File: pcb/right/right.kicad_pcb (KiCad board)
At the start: 2 copper layers, 33 x 71.1 mm, 21 parts

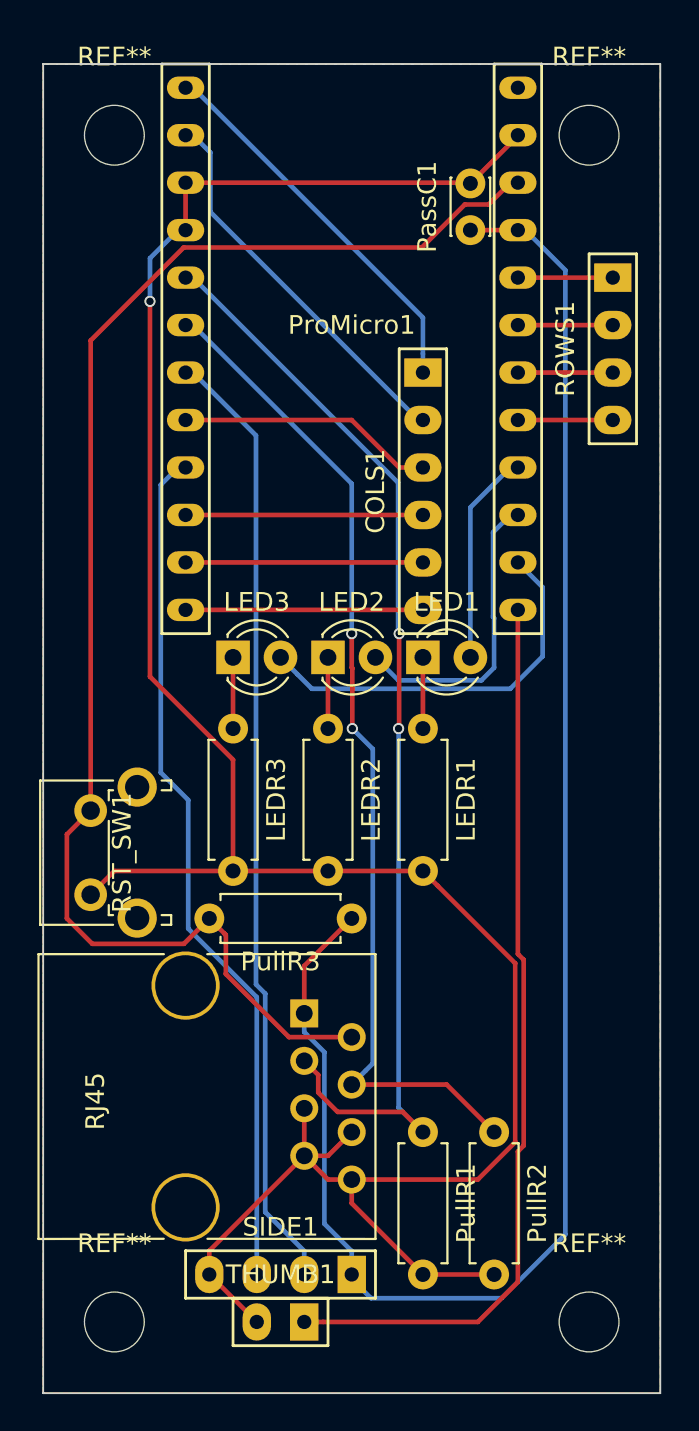
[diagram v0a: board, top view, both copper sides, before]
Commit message: fix pcb size
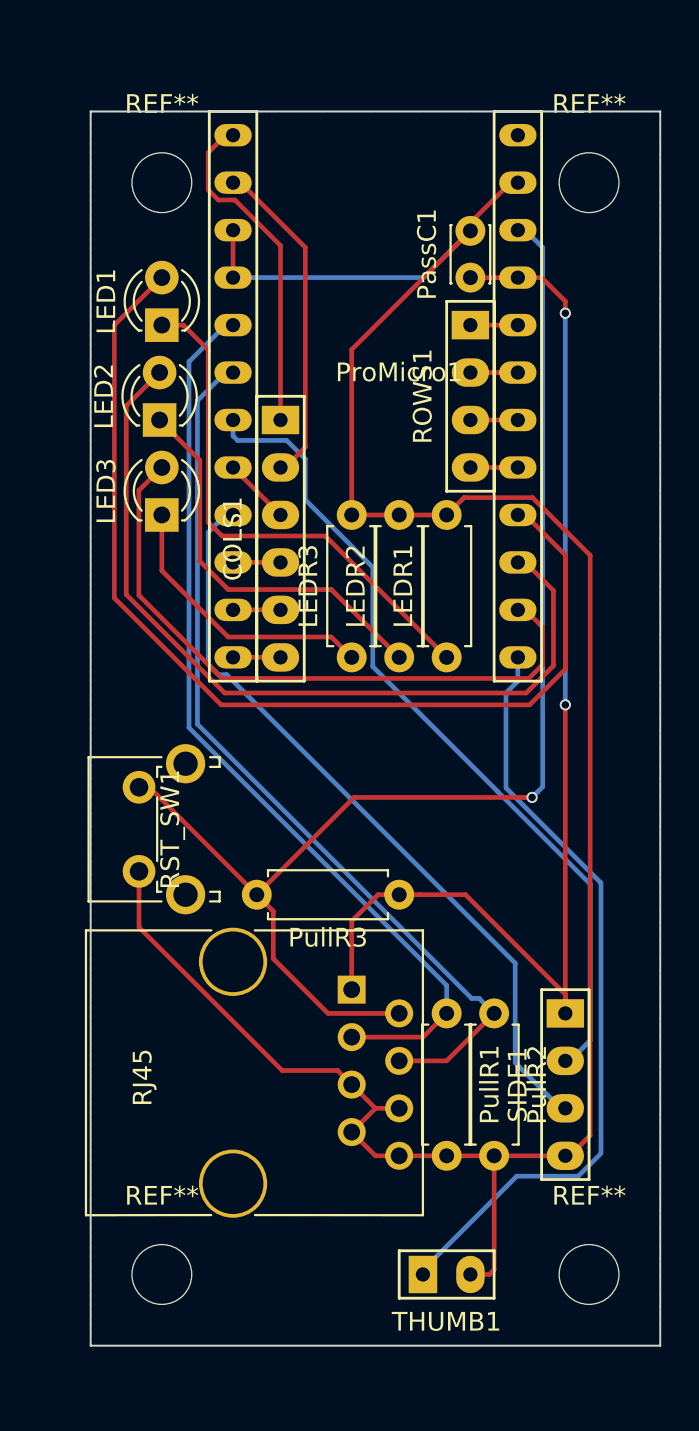
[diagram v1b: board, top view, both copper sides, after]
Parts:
- removed the REF** at (0.00, 0.00)
- removed the REF** at (25.4, 0.00)
- removed the REF** at (0.00, 63.5)
- removed the REF** at (25.4, 63.5)
- added REF**: MountingHole_3.2mm_M3, Mounting_Holes:MountingHole_3.2mm_M3, F.Cu at (2.54, 2.54)
- added REF**: MountingHole_3.2mm_M3, Mounting_Holes:MountingHole_3.2mm_M3, F.Cu at (25.4, 2.54)
- added REF**: MountingHole_3.2mm_M3, Mounting_Holes:MountingHole_3.2mm_M3, F.Cu at (2.54, 61.0)
- added REF**: MountingHole_3.2mm_M3, Mounting_Holes:MountingHole_3.2mm_M3, F.Cu at (25.4, 61.0)
- moved LED1 22.6 mm to (2.54, 10.2), turned to 90 degrees
- moved SIDE1 18.3 mm to (24.1, 50.8), turned to 0 degrees
- moved LED2 15.6 mm to (2.42, 15.2), turned to 90 degrees
- moved THUMB1 9.25 mm to (17.8, 61.0), turned to 90 degrees
- moved LED3 8.52 mm to (2.54, 20.3), turned to 90 degrees
- moved ROWS1 8.03 mm to (19.1, 14.0)
- moved COLS1 8.03 mm to (8.89, 21.6)
- moved LEDR3 7.41 mm to (12.7, 27.9), turned to 90 degrees
- moved PullR1 6.48 mm to (17.8, 47.0)
- moved PullR2 6.35 mm to (20.3, 47.0)
- moved LEDR2 5.39 mm to (15.2, 27.9), turned to 90 degrees
- moved LEDR1 4.02 mm to (17.8, 27.9), turned to 90 degrees
- moved ProMicro1 3.59 mm to (15.2, 14.0)
- moved RST_SW1 2.88 mm to (1.32, 39.4)
- moved RJ45 2.84 mm to (12.7, 45.7)
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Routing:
- net /LED1: track 11.4 -> 55.0 mm
- net +5V: track 92.2 -> 62.6 mm, vias 0 -> 2
- net /LED2: track 16.1 -> 44.8 mm
- net Net-(LED1-Pad1): track 3.81 -> 28.0 mm
- net Net-(LED2-Pad1): track 3.81 -> 21.2 mm
- net /LED3: track 21.0 -> 34.8 mm
- net Net-(LED3-Pad1): track 3.81 -> 15.1 mm
- net /SDA: track 59.7 -> 49.4 mm, vias 2 -> 0
- net /COL2: track 13.8 -> 3.59 mm
- net /COL5: track 12.7 -> 2.54 mm
- net /COL4: track 12.7 -> 2.54 mm
- net /COL3: track 12.7 -> 2.54 mm
- net /RST: track 78.0 -> 68.7 mm, vias 0 -> 1
- net /Thumb_key: track 48.5 -> 41.3 mm
- net GND: track 134.2 -> 127.4 mm, vias 1 -> 0
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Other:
- board size 33 x 71.1 mm -> 30.5 x 66 mm

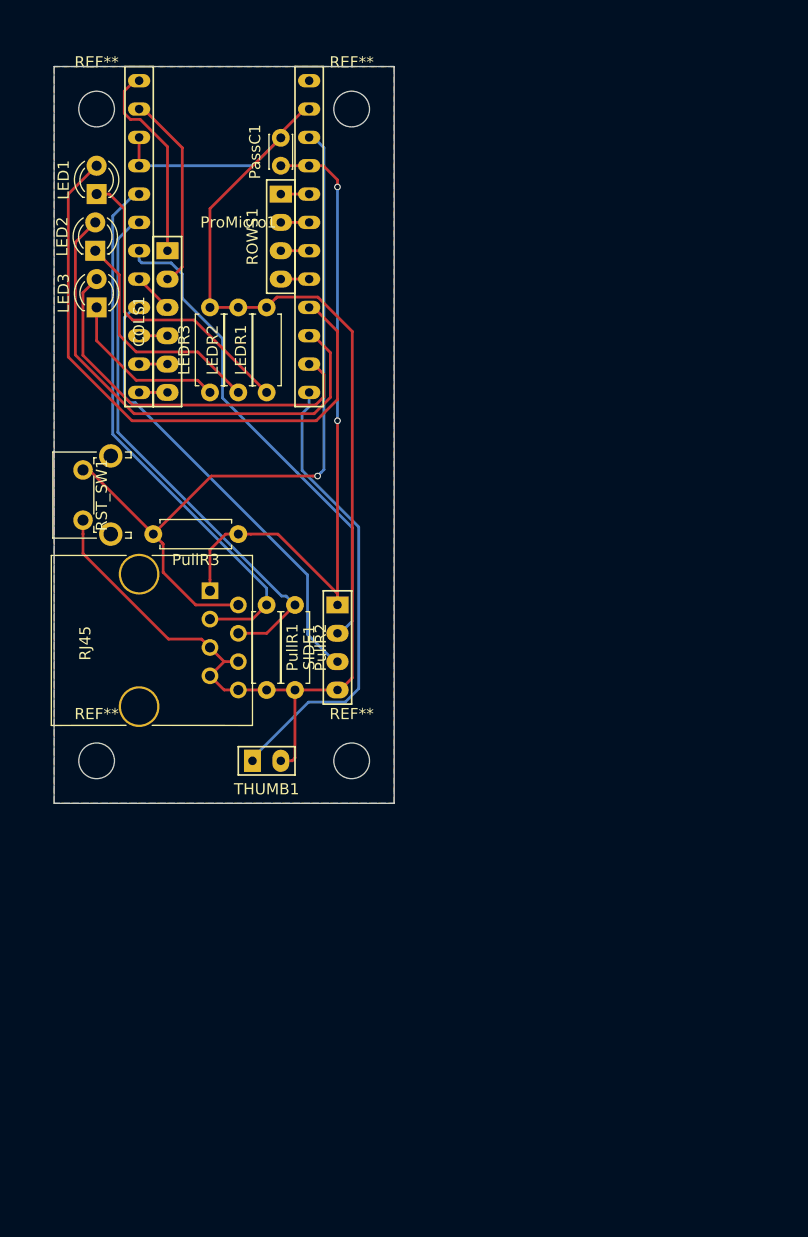
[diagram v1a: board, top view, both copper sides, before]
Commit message: improve parts arrangement
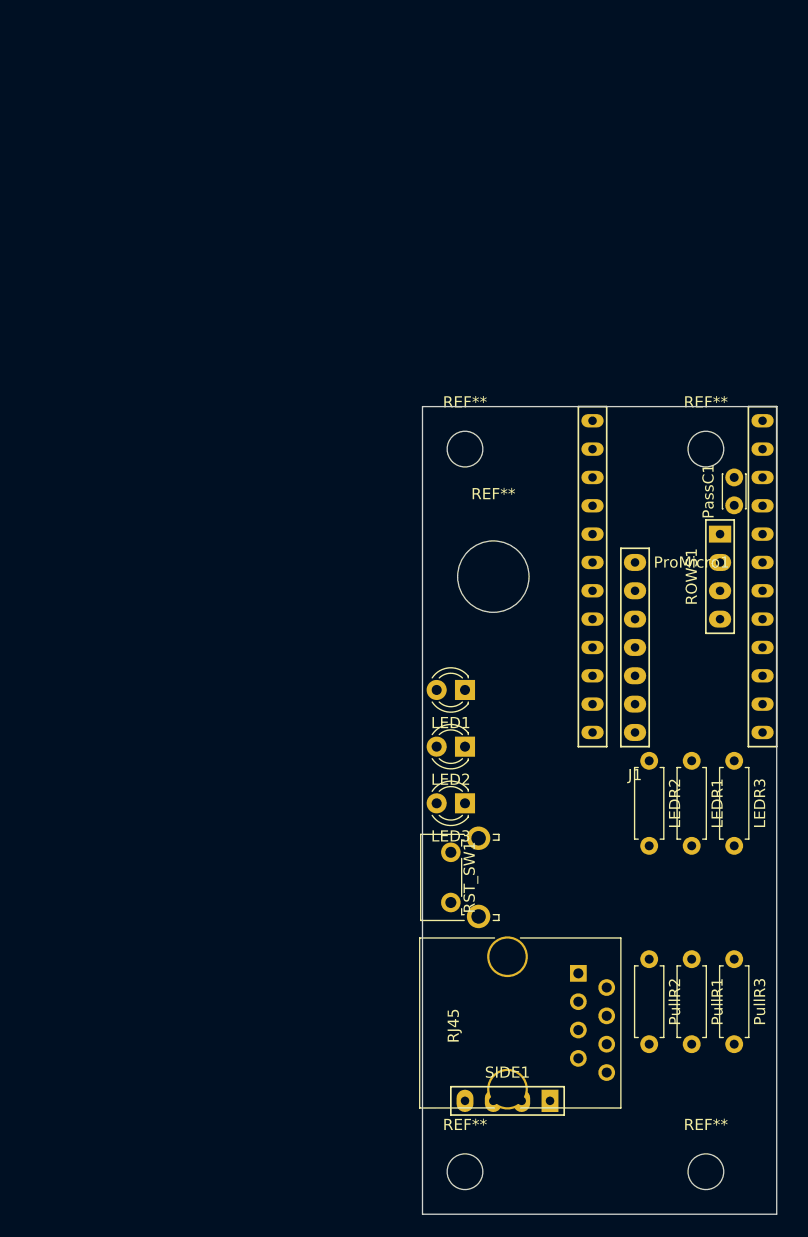
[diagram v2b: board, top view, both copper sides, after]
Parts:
- removed COLS1: Conn_01x06, 4x6t2:Wirepad_01x06
- removed the REF** at (2.54, 2.54)
- removed the REF** at (25.4, 2.54)
- removed the REF** at (2.54, 61.0)
- removed the REF** at (25.4, 61.0)
- removed THUMB1: Conn_01x02, 4x6t2:Wirepad_01x02
- added J1: Conn_01x07, 4x6t2:Wirepad_01x07, F.Cu at (50.8, 57.1)
- added REF**: MountingHole_3.2mm_M3, Mounting_Holes:MountingHole_3.2mm_M3, F.Cu at (57.1, 33.0)
- added REF**: MountingHole_6.4mm_M6, Mounting_Holes:MountingHole_6.4mm_M6, F.Cu at (38.1, 44.5)
- added REF**: MountingHole_3.2mm_M3, Mounting_Holes:MountingHole_3.2mm_M3, F.Cu at (57.1, 97.8)
- added REF**: MountingHole_3.2mm_M3, Mounting_Holes:MountingHole_3.2mm_M3, F.Cu at (35.6, 33.0)
- added REF**: MountingHole_3.2mm_M3, Mounting_Holes:MountingHole_3.2mm_M3, F.Cu at (35.6, 97.8)
- moved PullR3 58.5 mm to (59.7, 78.7), turned to 270 degrees
- moved LEDR3 57.4 mm to (59.7, 61.0), turned to 270 degrees
- moved LED2 55.4 mm to (35.6, 59.7), turned to 180 degrees
- moved LED1 55.4 mm to (35.6, 54.6), turned to 180 degrees
- moved LED3 55.4 mm to (35.6, 64.8), turned to 180 degrees
- moved ProMicro1 50.8 mm to (55.9, 44.5)
- moved PassC1 50.8 mm to (59.7, 38.1)
- moved LEDR1 50.4 mm to (55.9, 61.0), turned to 270 degrees
- moved ROWS1 49.8 mm to (58.4, 44.5)
- moved PullR1 49.6 mm to (55.9, 78.7)
- moved LEDR2 49.5 mm to (52.1, 61.0), turned to 270 degrees
- moved RJ45 47.6 mm to (45.7, 80.0)
- moved RST_SW1 47.6 mm to (34.3, 73.7)
- moved PullR2 44.9 mm to (52.1, 78.7)
- moved SIDE1 43.4 mm to (39.4, 91.4), turned to 270 degrees
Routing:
- net GND: track 127.4 -> 0.00 mm
- net /RST: track 68.7 -> 0.00 mm, vias 1 -> 0
- net +5V: track 62.6 -> 0.00 mm, vias 2 -> 0
- net /LED1: track 55.0 -> 0.00 mm
- net /SDA: track 49.4 -> 0.00 mm
- net /SCL: track 48.3 -> 0.00 mm
- net /LED2: track 44.8 -> 0.00 mm
- net /X: track 44.4 -> 0.00 mm
- net /Thumb_key: track 41.3 -> 0.00 mm
- net /Y: track 40.9 -> 0.00 mm
- net /LED3: track 34.8 -> 0.00 mm
- net Net-(LED1-Pad1): track 28.0 -> 0.00 mm
- net Net-(LED2-Pad1): track 21.2 -> 0.00 mm
- net /COL0: track 18.1 -> 0.00 mm
- net /COL1: track 17.8 -> 0.00 mm
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- removed copper zone on B.Cu, net GND
- removed copper zone on F.Cu, net GND
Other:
- board size 30.5 x 66 mm -> 31.8 x 72.4 mm

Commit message: improve pcb size
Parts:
- moved SIDE1 10.2 mm to (48.3, 96.5)
- moved PullR2 3.81 mm to (55.9, 78.7)
- moved RJ45 3.81 mm to (49.5, 80.0)
- moved RST_SW1 3.81 mm to (38.1, 73.7)
- moved LED1 3.81 mm to (39.4, 54.6)
- moved LED2 3.81 mm to (39.4, 59.7)
- moved LED3 3.81 mm to (39.4, 64.8)
- moved REF** 3.81 mm to (41.9, 44.5)
- moved REF** 3.81 mm to (39.4, 33.0)
- moved REF** 3.81 mm to (39.4, 97.8)
- moved PullR1 2.54 mm to (58.4, 78.7)
- moved PullR3 1.27 mm to (61.0, 78.7)
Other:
- board size 31.8 x 72.4 mm -> 27.9 x 72.4 mm
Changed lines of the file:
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@@
     (links 44)
     (no_connects 44)
-    (area 28.539857 27.842 66.710143 103.068)
+    (area 29.809857 27.842 66.710143 103.068)
     (thickness 1.6)
     (drawings 4)
@@
   )
   (module LEDs:LED_D3.0mm (layer F.Cu)
-    (at 35.56 54.61 180)
+    (at 39.37 54.61 180)
     (descr "LED, diameter 3.0mm, 2 pins")
     (tags "LED diameter 3.0mm 2 pins")
@@
   )
   (module LEDs:LED_D3.0mm (layer F.Cu)
-    (at 35.56 59.69 180)
+    (at 39.37 59.69 180)
     (descr "LED, diameter 3.0mm, 2 pins")
     (tags "LED diameter 3.0mm 2 pins")
@@
   )
   (module LEDs:LED_D3.0mm (layer F.Cu)
-    (at 35.56 64.77 180)
+    (at 39.37 64.77 180)
     (descr "LED, diameter 3.0mm, 2 pins")
     (tags "LED diameter 3.0mm 2 pins")
@@
   )
   (module Resistors_THT:R_Axial_DIN0207_L6.3mm_D2.5mm_P7.62mm_Horizontal (layer F.Cu)
-    (at 55.88 78.74 270)
+    (at 58.42 78.74 270)
     (descr "Resistor, Axial_DIN0207 series, Axial, Horizontal, pin pitch=7.62mm, 0.25W = 1/4W, length*diameter=6.3*2.5mm^2, http://cdn-reichelt.de/documents/datenblatt/B400/1_4W%23YAG.pdf")
     (tags "Resistor Axial_DIN0207 series Axial Horizontal pin pitch 7.62mm 0.25W = 1/4W length 6.3mm diameter 2.5mm")
@@
   )
   (module Resistors_THT:R_Axial_DIN0207_L6.3mm_D2.5mm_P7.62mm_Horizontal (layer F.Cu)
-    (at 52.07 78.74 270)
+    (at 55.88 78.74 270)
     (descr "Resistor, Axial_DIN0207 series, Axial, Horizontal, pin pitch=7.62mm, 0.25W = 1/4W, length*diameter=6.3*2.5mm^2, http://cdn-reichelt.de/documents/datenblatt/B400/1_4W%23YAG.pdf")
     (tags "Resistor Axial_DIN0207 series Axial Horizontal pin pitch 7.62mm 0.25W = 1/4W length 6.3mm diameter 2.5mm")
@@
   )
   (module Resistors_THT:R_Axial_DIN0207_L6.3mm_D2.5mm_P7.62mm_Horizontal (layer F.Cu)
-    (at 59.69 78.74 270)
+    (at 60.96 78.74 270)
     (descr "Resistor, Axial_DIN0207 series, Axial, Horizontal, pin pitch=7.62mm, 0.25W = 1/4W, length*diameter=6.3*2.5mm^2, http://cdn-reichelt.de/documents/datenblatt/B400/1_4W%23YAG.pdf")
     (tags "Resistor Axial_DIN0207 series Axial Horizontal pin pitch 7.62mm 0.25W = 1/4W length 6.3mm diameter 2.5mm")
@@
   )
   (module Connectors:RJ45_8 (layer F.Cu)
-    (at 45.72 80.01 270)
+    (at 49.53 80.01 270)
     (tags RJ45)
     (fp_text reference RJ45 (at 4.7 11.18 270) (layer F.SilkS)
@@
   )
   (module Buttons_Switches_THT:SW_Tactile_SPST_Angled_PTS645Vx31-2LFS (layer F.Cu)
-    (at 34.29 73.66 90)
+    (at 38.1 73.66 90)
     (descr "tactile switch SPST right angle, PTS645VL31-2 LFS")
     (tags "tactile switch SPST angled PTS645VL31-2 LFS C&K Button")
@@
   )
   (module 4x6t2:Wirepad_01x04 (layer F.Cu)
-    (at 39.37 91.44 270)
+    (at 48.26 96.52 270)
     (fp_text reference SIDE1 (at -2.54 0 360) (layer F.SilkS)
       (effects (font (size 1 1) (thickness 0.15)))
@@
   )
   (module Mounting_Holes:MountingHole_6.4mm_M6 (layer F.Cu)
-    (at 38.1 44.45)
+    (at 41.91 44.45)
     (descr "Mounting Hole 6.4mm, no annular, M6")
     (tags "mounting hole 6.4mm no annular m6")
@@
   )
   (module Mounting_Holes:MountingHole_3.2mm_M3 (layer F.Cu)
-    (at 35.56 33.02)
+    (at 39.37 33.02)
     (descr "Mounting Hole 3.2mm, no annular, M3")
     (tags "mounting hole 3.2mm no annular m3")
@@
   )
   (module Mounting_Holes:MountingHole_3.2mm_M3 (layer F.Cu)
-    (at 35.56 97.79)
+    (at 39.37 97.79)
     (descr "Mounting Hole 3.2mm, no annular, M3")
     (tags "mounting hole 3.2mm no annular m3")
@@
       (net 6 /COL5))
   )
-  (gr_line (start 31.75 101.6) (end 63.5 101.6) (layer Edge.Cuts) (width 0.1))
+  (gr_line (start 35.56 101.6) (end 63.5 101.6) (layer Edge.Cuts) (width 0.1))
   (gr_line (start 63.5 29.21) (end 63.5 101.6) (layer Edge.Cuts) (width 0.1))
-  (gr_line (start 31.75 29.21) (end 31.75 101.6) (layer Edge.Cuts) (width 0.1))
-  (gr_line (start 63.5 29.21) (end 31.75 29.21) (layer Edge.Cuts) (width 0.1))
+  (gr_line (start 35.56 29.21) (end 35.56 101.6) (layer Edge.Cuts) (width 0.1))
+  (gr_line (start 63.5 29.21) (end 35.56 29.21) (layer Edge.Cuts) (width 0.1))
 )

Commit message: connect pad
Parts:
- moved LEDR3 10.8 mm to (52.1, 68.6), turned to 90 degrees
- moved LEDR2 8.52 mm to (55.9, 68.6), turned to 90 degrees
- moved LEDR1 8.52 mm to (59.7, 68.6), turned to 90 degrees
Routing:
- net GND: track 0.00 -> 136.7 mm, vias 0 -> 1
- net /RST: track 0.00 -> 86.1 mm
- net +5V: track 0.00 -> 83.0 mm
- net /X: track 0.00 -> 58.2 mm
- net /SDA: track 0.00 -> 56.3 mm
- net /Y: track 0.00 -> 47.1 mm
- net /SCL: track 0.00 -> 46.1 mm
- net /LED3: track 0.00 -> 40.3 mm
- net /LED2: track 0.00 -> 31.8 mm
- net /LED1: track 0.00 -> 27.7 mm
- net Net-(LED1-Pad1): track 0.00 -> 26.1 mm
- net /Thumb_key: track 0.00 -> 20.3 mm, vias 0 -> 1
- net Net-(LED2-Pad1): track 0.00 -> 20.2 mm
- net /COL1: track 0.00 -> 17.8 mm
- net /COL0: track 0.00 -> 17.2 mm
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- added copper zone on B.Cu, net GND
- added copper zone on F.Cu, net GND
